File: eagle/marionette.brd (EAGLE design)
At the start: 112.4 x 100 mm, 40 parts, among them J2 SWD_CONNECTOR, U1 USB3318, U2 NCP705, U3 XCL206B, X1 ABS25-32.768KHZ-6-T

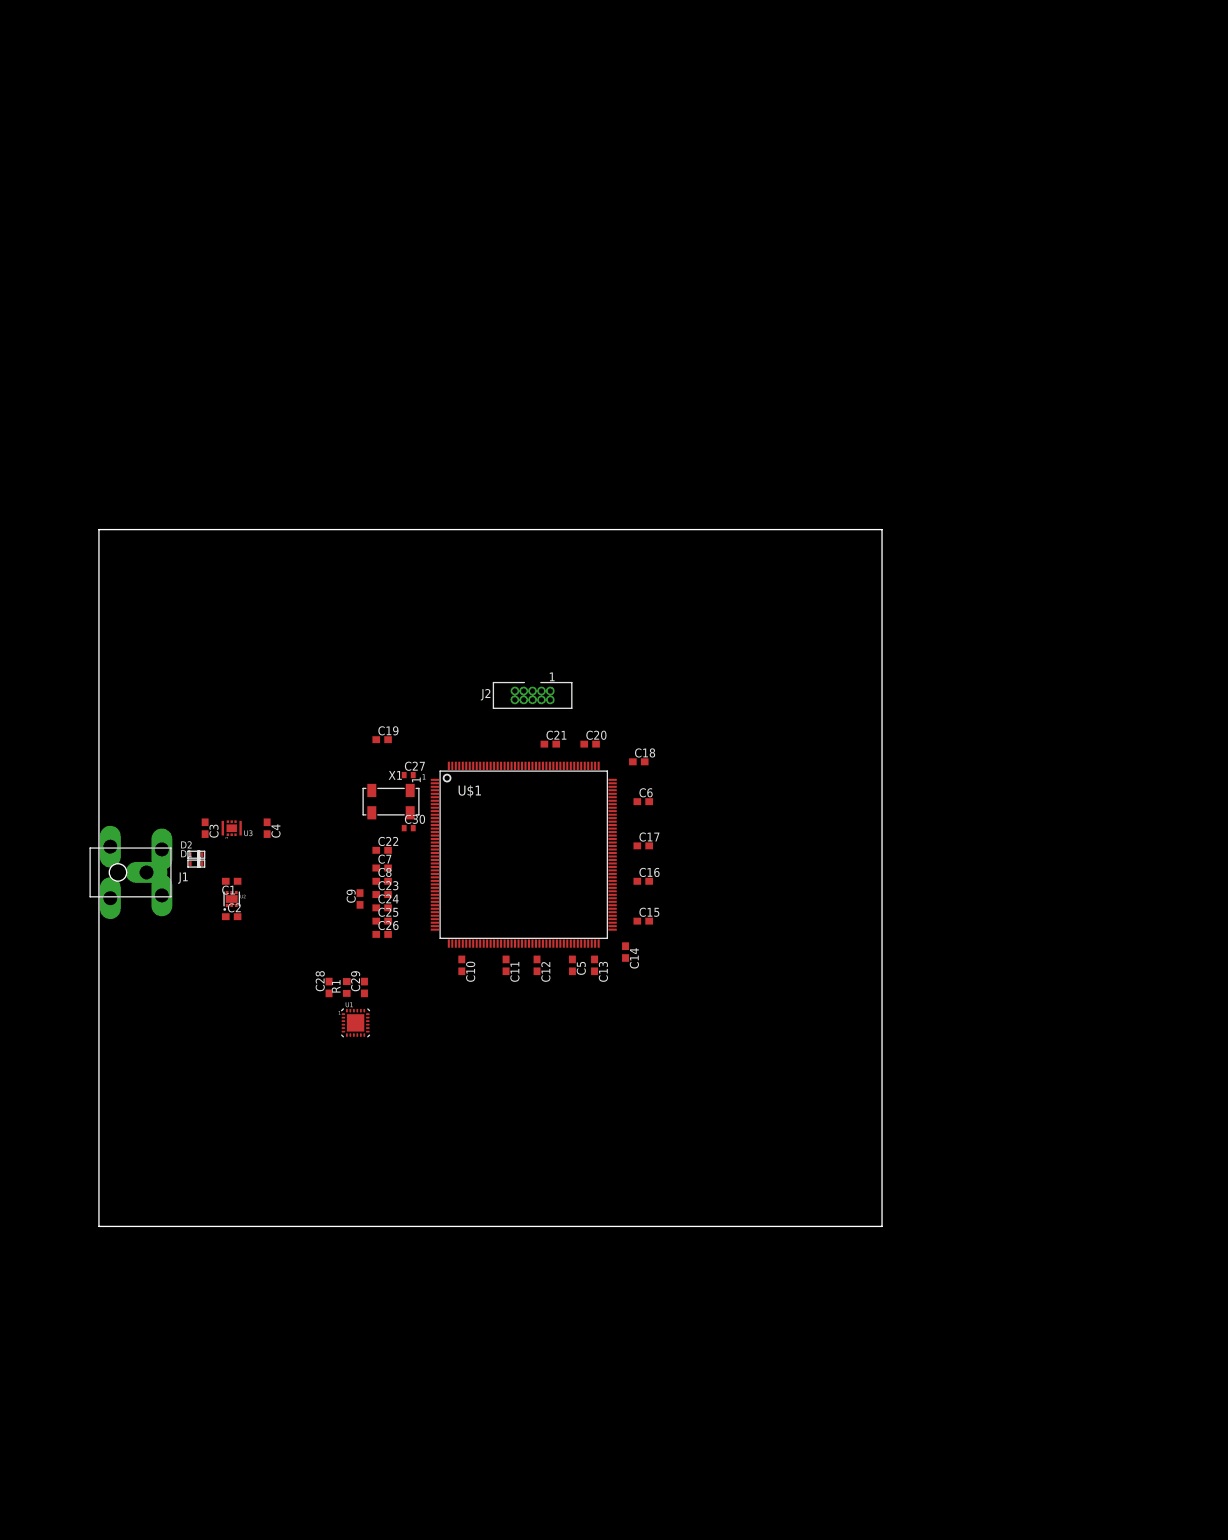
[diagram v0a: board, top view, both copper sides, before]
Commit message: Added 20pin connectors
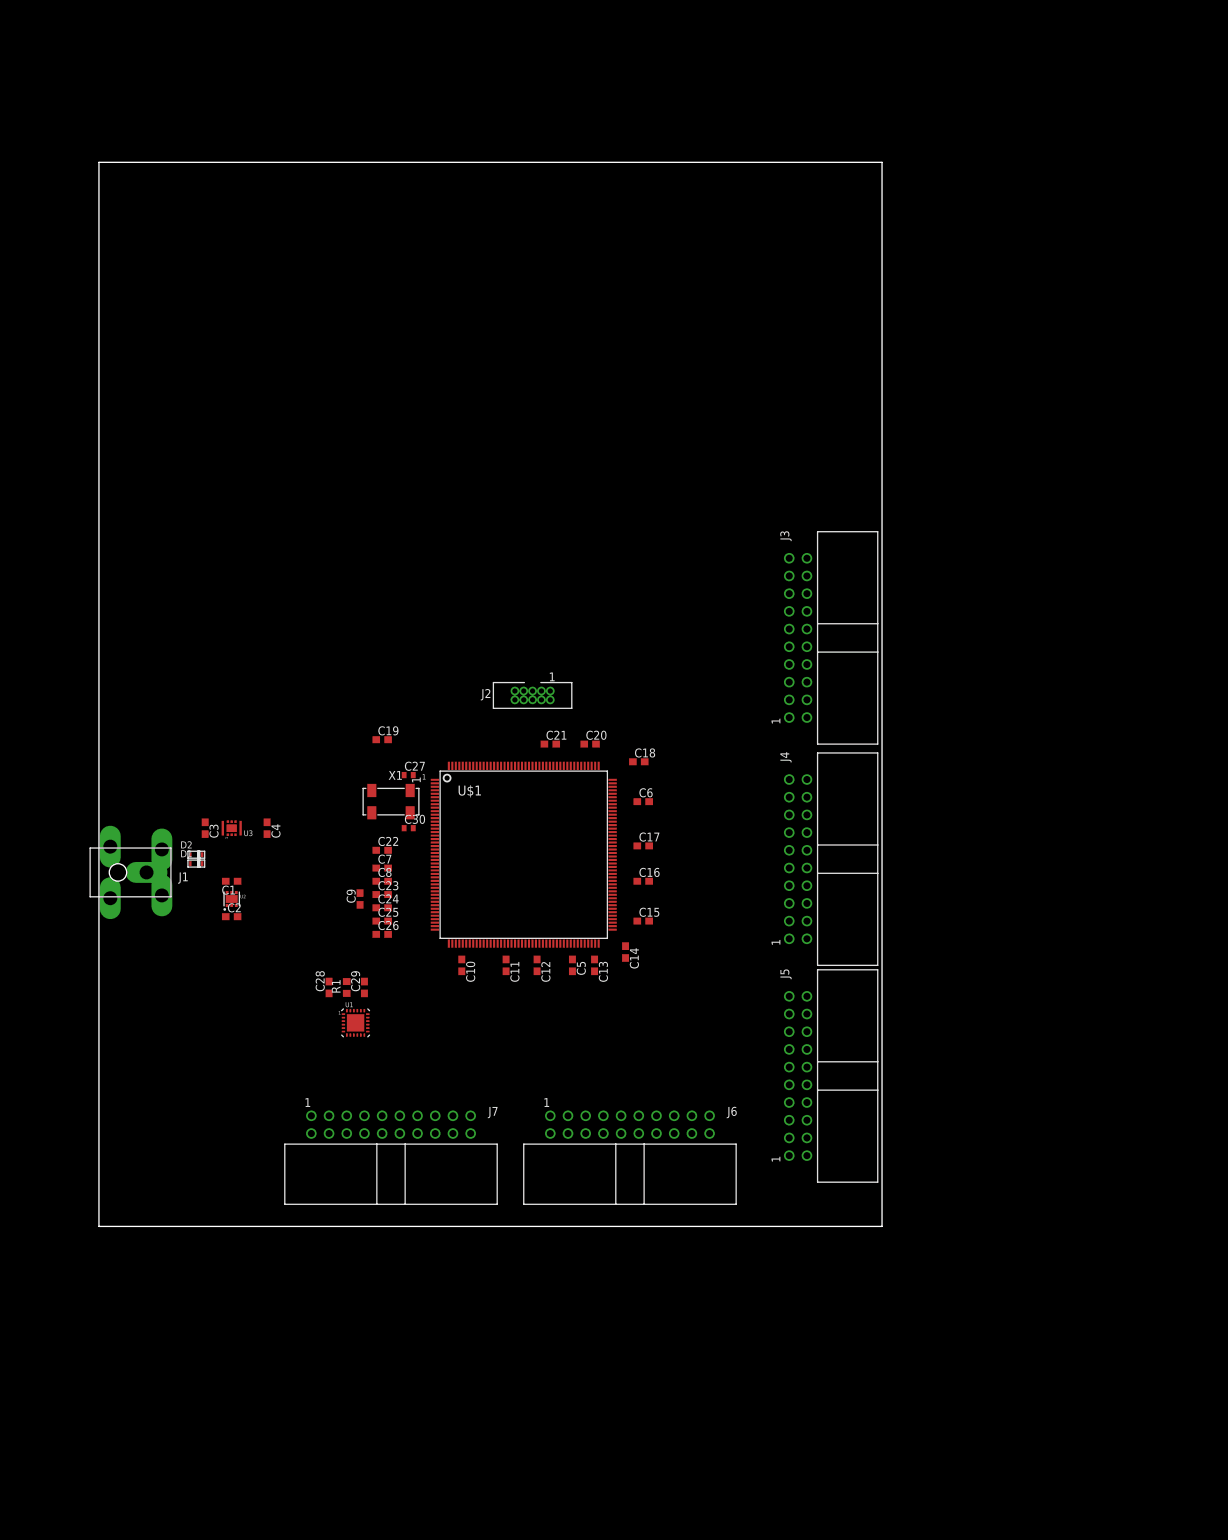
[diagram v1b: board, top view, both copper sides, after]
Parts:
- added J3, J4, J5, J6, J7: 2X10FE, 20POS_ANGLED_FEMALE_HEADER:2X10_FEMALE_ANGLED
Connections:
- net GND: now also J3.20, J4.20, J5.20, J6.20, J7.20
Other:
- board size 112.4 x 100 mm -> 112.4 x 152.7 mm
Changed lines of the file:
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@@
 <setting verticaltext="up"/>
 </settings>
-<grid distance="0.025" unitdist="inch" unit="inch" style="lines" multiple="1" display="no" altdistance="0.025" altunitdist="inch" altunit="inch"/>
+<grid distance="0.025" unitdist="inch" unit="inch" style="lines" multiple="1" display="yes" altdistance="0.025" altunitdist="inch" altunit="inch"/>
 <layers>
 <layer number="1" name="Top" color="4" fill="1" visible="yes" active="yes"/>
@@
 <plain>
 <wire x1="0" y1="0" x2="112.375" y2="0" width="0" layer="20"/>
-<wire x1="112.375" y1="0" x2="112.375" y2="100" width="0" layer="20"/>
-<wire x1="112.375" y1="100" x2="0" y2="100" width="0" layer="20"/>
-<wire x1="0" y1="100" x2="0" y2="0" width="0" layer="20"/>
+<wire x1="112.375" y1="0" x2="112.375" y2="152.705" width="0" layer="20"/>
+<wire x1="112.375" y1="152.705" x2="0" y2="152.705" width="0" layer="20"/>
+<wire x1="0" y1="152.705" x2="0" y2="0" width="0" layer="20"/>
 </plain>
 <attributes>
@@
 <element name="U3" library="XCL206B" package="56-BCPGA" value="XCL206B" x="19.05" y="57.15"/>
 <element name="X1" library="ABS25" package="4-SOJ" value="ABS25-32.768KHZ-6-T" x="41.91" y="60.96" rot="R180"/>
+<element name="J3" library="20POS_ANGLED_FEMALE_HEADER" package="2X10_FEMALE_ANGLED" value="2X10FE" x="100.33" y="84.455" rot="R90"/>
+<element name="J4" library="20POS_ANGLED_FEMALE_HEADER" package="2X10_FEMALE_ANGLED" value="2X10FE" x="100.33" y="52.705" rot="R90"/>
+<element name="J5" library="20POS_ANGLED_FEMALE_HEADER" package="2X10_FEMALE_ANGLED" value="2X10FE" x="100.33" y="21.59" rot="R90"/>
+<element name="J6" library="20POS_ANGLED_FEMALE_HEADER" package="2X10_FEMALE_ANGLED" value="2X10FE" x="76.2" y="14.605"/>
+<element name="J7" library="20POS_ANGLED_FEMALE_HEADER" package="2X10_FEMALE_ANGLED" value="2X10FE" x="41.91" y="14.605"/>
 </elements>
 <signals>
@@
 <contactref element="C5" pad="2"/>
 <contactref element="C6" pad="2"/>
+<contactref element="J7" pad="20"/>
+<contactref element="J6" pad="20"/>
+<contactref element="J5" pad="20"/>
+<contactref element="J4" pad="20"/>
+<contactref element="J3" pad="20"/>
 <wire x1="78.955" y1="60.96" x2="78.32" y2="66.675" width="0" layer="19" extent="1-1"/>
 <wire x1="73.71" y1="61.09" x2="78.955" y2="60.96" width="0" layer="19" extent="1-1"/>
@@
 <wire x1="19.71" y1="46.065" x2="19.05" y2="46.99" width="0" layer="19" extent="1-1"/>
 <wire x1="19.9" y1="44.45" x2="19.71" y2="46.065" width="0" layer="19" extent="1-1"/>
+<wire x1="101.6" y1="95.885" x2="52.07" y2="36.615" width="0" layer="19" extent="1-1"/>
+<wire x1="101.6" y1="64.135" x2="101.6" y2="95.885" width="0" layer="19" extent="1-1"/>
+<wire x1="101.6" y1="33.02" x2="101.6" y2="64.135" width="0" layer="19" extent="1-1"/>
+<wire x1="87.63" y1="13.335" x2="101.6" y2="33.02" width="0" layer="19" extent="1-1"/>
+<wire x1="53.34" y1="13.335" x2="87.63" y2="13.335" width="0" layer="19" extent="1-1"/>
 </signal>
 <signal name="SDIO_D4">

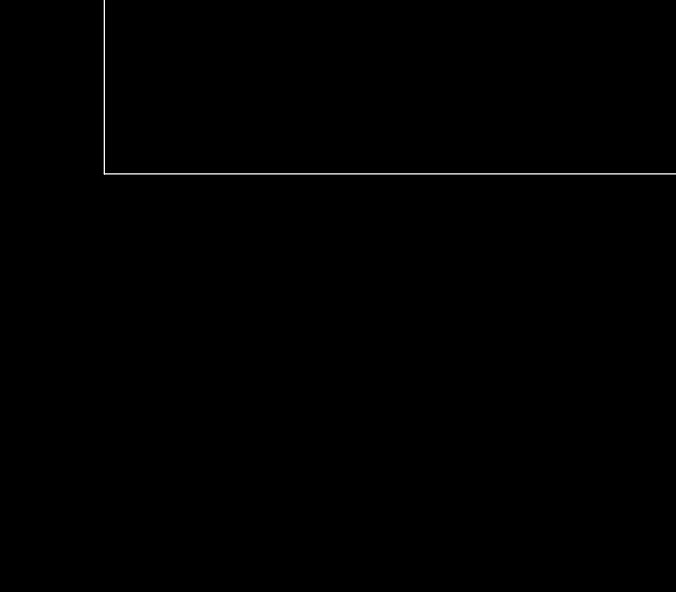
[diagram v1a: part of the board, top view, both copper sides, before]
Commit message: Added micro USB connectors
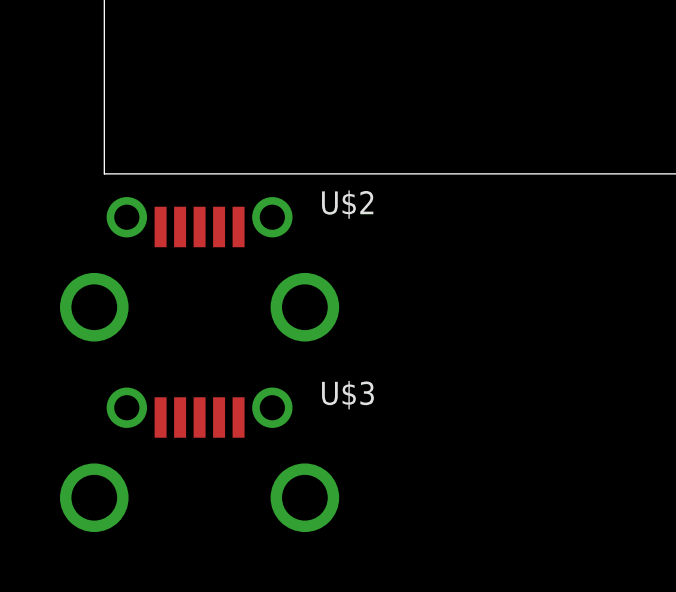
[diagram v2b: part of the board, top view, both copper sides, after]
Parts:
- added U$2, U$3: ZX62D-B-5P8, con-hirose-microusb:ZX62D-B-5P8
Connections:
- removed net N$13: U$1.122
- removed net N$14: U$1.123
- removed net N$2: U$1.120
- removed net N$6: U$1.121
- new net FS_DM: U$1.122, U$2.P2
- new net FS_DP: U$1.123, U$2.P3
- new net FS_ID: U$1.121, U$2.P4
- new net OTG_VBUS: D2.P$1, U$1.120, U$2.P1
- new net SHLD: U$3.P$1, U$3.P$2, U$3.P$3, U$3.P$4
- new net VCC: U$3.P1
- net GND: now also U$2.P$1, U$2.P$2, U$2.P$3, U$2.P$4, U$2.P5
- net N$12: now also U$3.P5
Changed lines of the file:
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@@
 <layer number="54" name="bGND_GNDA" color="1" fill="9" visible="no" active="no"/>
 <layer number="56" name="wert" color="7" fill="1" visible="no" active="no"/>
+<layer number="59" name="Invisible" color="7" fill="1" visible="yes" active="yes"/>
+<layer number="61" name="stand" color="7" fill="1" visible="yes" active="yes"/>
 <layer number="90" name="Modules" color="5" fill="1" visible="no" active="no"/>
 <layer number="91" name="Nets" color="2" fill="1" visible="no" active="no"/>
@@
 <layer number="107" name="Crop" color="7" fill="1" visible="no" active="yes"/>
 <layer number="108" name="dxf_notes" color="14" fill="1" visible="yes" active="yes"/>
+<layer number="109" name="fp9" color="7" fill="1" visible="yes" active="yes"/>
 <layer number="110" name="labels" color="7" fill="1" visible="yes" active="yes"/>
 <layer number="111" name="print" color="7" fill="1" visible="yes" active="yes"/>
@@
 <layer number="121" name="_tsilk" color="7" fill="1" visible="no" active="yes"/>
 <layer number="122" name="_bsilk" color="7" fill="1" visible="no" active="yes"/>
+<layer number="123" name="tTestmark" color="7" fill="1" visible="yes" active="yes"/>
+<layer number="124" name="bTestmark" color="7" fill="1" visible="yes" active="yes"/>
 <layer number="125" name="_tNames" color="7" fill="1" visible="no" active="yes"/>
+<layer number="126" name="_bNames" color="7" fill="1" visible="yes" active="yes"/>
+<layer number="127" name="_tValues" color="7" fill="1" visible="yes" active="yes"/>
+<layer number="128" name="_bValues" color="7" fill="1" visible="yes" active="yes"/>
+<layer number="130" name="bLogo" color="7" fill="1" visible="yes" active="yes"/>
+<layer number="131" name="tText" color="7" fill="1" visible="yes" active="yes"/>
+<layer number="132" name="bMask" color="7" fill="1" visible="yes" active="yes"/>
 <layer number="144" name="Drill_legend" color="7" fill="1" visible="no" active="yes"/>
 <layer number="151" name="HeatSink" color="7" fill="1" visible="no" active="yes"/>
+<layer number="152" name="_bDocu" color="7" fill="1" visible="yes" active="yes"/>
+<layer number="199" name="Contour" color="7" fill="1" visible="yes" active="yes"/>
 <layer number="200" name="200bmp" color="1" fill="10" visible="no" active="yes"/>
 <layer number="201" name="201bmp" color="2" fill="10" visible="no" active="yes"/>
@@
 <layer number="223" name="223bmp" color="24" fill="1" visible="no" active="no"/>
 <layer number="224" name="224bmp" color="25" fill="1" visible="no" active="no"/>
+<layer number="225" name="225bmp" color="7" fill="1" visible="yes" active="yes"/>
+<layer number="226" name="226bmp" color="7" fill="1" visible="yes" active="yes"/>
+<layer number="227" name="227bmp" color="7" fill="1" visible="yes" active="yes"/>
+<layer number="228" name="228bmp" color="7" fill="1" visible="yes" active="yes"/>
+<layer number="231" name="Eagle3D_PG1" color="7" fill="1" visible="yes" active="yes"/>
+<layer number="232" name="Eagle3D_PG2" color="7" fill="1" visible="yes" active="yes"/>
+<layer number="233" name="Eagle3D_PG3" color="7" fill="1" visible="yes" active="yes"/>
+<layer number="248" name="Housing" color="7" fill="1" visible="yes" active="yes"/>
+<layer number="249" name="Edge" color="7" fill="1" visible="yes" active="yes"/>
 <layer number="250" name="Descript" color="3" fill="1" visible="no" active="no"/>
 <layer number="251" name="SMDround" color="12" fill="11" visible="no" active="no"/>
@@
 <element name="J6" library="20POS_ANGLED_FEMALE_HEADER" package="2X10_FEMALE_ANGLED" value="2X10FE" x="76.2" y="14.605"/>
 <element name="J7" library="20POS_ANGLED_FEMALE_HEADER" package="2X10_FEMALE_ANGLED" value="2X10FE" x="41.91" y="14.605"/>
+<element name="U$2" library="con-hirose-microusb" package="ZX62D-B-5P8" value="ZX62D-B-5P8" x="3.175" y="-4.445"/>
+<element name="U$3" library="con-hirose-microusb" package="ZX62D-B-5P8" value="ZX62D-B-5P8" x="3.175" y="-10.795"/>
 </elements>
 <signals>
@@
 <contactref element="C28" pad="2"/>
 <contactref element="C29" pad="2"/>
+<contactref element="U$3" pad="P5"/>
 <wire x1="35.56" y1="35.14" x2="38.1" y2="35.14" width="0" layer="19" extent="1-1"/>
 <wire x1="33.02" y1="35.14" x2="35.56" y2="35.14" width="0" layer="19" extent="1-1"/>
 <wire x1="36.83" y1="29.21" x2="38.1" y2="35.14" width="0" layer="19" extent="1-1"/>
+<wire x1="4.475" y1="-8.12" x2="36.83" y2="29.21" width="0" layer="19" extent="1-1"/>
 </signal>
 <signal name="N$7">
@@
 <contactref element="J4" pad="20"/>
 <contactref element="J3" pad="20"/>
-<wire x1="78.955" y1="60.96" x2="78.32" y2="66.675" width="0" layer="19" extent="1-1"/>
+<contactref element="U$2" pad="P5"/>
+<contactref element="U$2" pad="P$1"/>
+<contactref element="U$2" pad="P$2"/>
+<contactref element="U$2" pad="P$3"/>
+<contactref element="U$2" pad="P$4"/>
+<wire x1="101.6" y1="64.135" x2="101.6" y2="95.885" width="0" layer="19" extent="1-1"/>
+<wire x1="78.955" y1="60.96" x2="101.6" y2="64.135" width="0" layer="19" extent="1-1"/>
 <wire x1="73.71" y1="61.09" x2="78.955" y2="60.96" width="0" layer="19" extent="1-1"/>
+<wire x1="78.32" y1="66.675" x2="78.955" y2="60.96" width="0" layer="19" extent="1-1"/>
 <wire x1="70.71" y1="66.09" x2="73.71" y2="61.09" width="0" layer="19" extent="1-1"/>
 <wire x1="71.335" y1="69.215" x2="70.71" y2="66.09" width="0" layer="19" extent="1-1"/>
@@
 <wire x1="19.71" y1="46.065" x2="19.05" y2="46.99" width="0" layer="19" extent="1-1"/>
 <wire x1="19.9" y1="44.45" x2="19.71" y2="46.065" width="0" layer="19" extent="1-1"/>
-<wire x1="101.6" y1="95.885" x2="52.07" y2="36.615" width="0" layer="19" extent="1-1"/>
-<wire x1="101.6" y1="64.135" x2="101.6" y2="95.885" width="0" layer="19" extent="1-1"/>
-<wire x1="101.6" y1="33.02" x2="101.6" y2="64.135" width="0" layer="19" extent="1-1"/>
+<wire x1="53.34" y1="13.335" x2="52.07" y2="36.615" width="0" layer="19" extent="1-1"/>
+<wire x1="101.6" y1="33.02" x2="78.955" y2="43.815" width="0" layer="19" extent="1-1"/>
 <wire x1="87.63" y1="13.335" x2="101.6" y2="33.02" width="0" layer="19" extent="1-1"/>
-<wire x1="53.34" y1="13.335" x2="87.63" y2="13.335" width="0" layer="19" extent="1-1"/>
+<wire x1="5.6" y1="-1.445" x2="19.9" y2="44.45" width="0" layer="19" extent="1-1"/>
+<wire x1="4.475" y1="-1.77" x2="5.6" y2="-1.445" width="0" layer="19" extent="1-1"/>
+<wire x1="6.685" y1="-4.445" x2="5.6" y2="-1.445" width="0" layer="19" extent="1-1"/>
+<wire x1="0.75" y1="-1.445" x2="4.475" y2="-1.77" width="0" layer="19" extent="1-1"/>
+<wire x1="-0.335" y1="-4.445" x2="0.75" y2="-1.445" width="0" layer="19" extent="1-1"/>
 </signal>
 <signal name="SDIO_D4">
@@
 <contactref element="U$1" pad="58"/>
 </signal>
-<signal name="N$2">
-<contactref element="U$1" pad="120"/>
-</signal>
-<signal name="N$6">
-<contactref element="U$1" pad="121"/>
-</signal>
-<signal name="N$13">
-<contactref element="U$1" pad="122"/>
-</signal>
-<signal name="N$14">
-<contactref element="U$1" pad="123"/>
-</signal>
 <signal name="PA15">
 <contactref element="U$1" pad="138"/>
@@
 <wire x1="18.2" y1="44.45" x2="18.39" y2="46.065" width="0" layer="19" extent="1-1"/>
 </signal>
+<signal name="SHLD">
+<contactref element="U$3" pad="P$1"/>
+<contactref element="U$3" pad="P$2"/>
+<contactref element="U$3" pad="P$3"/>
+<contactref element="U$3" pad="P$4"/>
+<wire x1="0.75" y1="-7.795" x2="-0.335" y2="-10.795" width="0" layer="19" extent="1-1"/>
+<wire x1="5.6" y1="-7.795" x2="0.75" y2="-7.795" width="0" layer="19" extent="1-1"/>
+<wire x1="6.685" y1="-10.795" x2="5.6" y2="-7.795" width="0" layer="19" extent="1-1"/>
+</signal>
+<signal name="VCC">
+<contactref element="U$3" pad="P1"/>
+</signal>
+<signal name="OTG_VBUS">
+<contactref element="U$1" pad="120"/>
+<contactref element="U$2" pad="P1"/>
+<contactref element="D2" pad="P$1"/>
+<wire x1="13.12" y1="53.34" x2="73.71" y2="58.09" width="0" layer="19" extent="1-1"/>
+<wire x1="1.875" y1="-1.77" x2="13.12" y2="53.34" width="0" layer="19" extent="1-1"/>
+</signal>
+<signal name="FS_ID">
+<contactref element="U$1" pad="121"/>
+<contactref element="U$2" pad="P4"/>
+<wire x1="3.825" y1="-1.77" x2="73.71" y2="58.59" width="0" layer="19" extent="1-1"/>
+</signal>
+<signal name="FS_DM">
+<contactref element="U$1" pad="122"/>
+<contactref element="U$2" pad="P2"/>
+<wire x1="2.525" y1="-1.77" x2="73.71" y2="59.09" width="0" layer="19" extent="1-1"/>
+</signal>
+<signal name="FS_DP">
+<contactref element="U$1" pad="123"/>
+<contactref element="U$2" pad="P3"/>
+<wire x1="3.175" y1="-1.77" x2="73.71" y2="59.59" width="0" layer="19" extent="1-1"/>
+</signal>
 </signals>
